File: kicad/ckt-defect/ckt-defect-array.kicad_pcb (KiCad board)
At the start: 2 copper layers, 114.3 x 188 mm, 307 parts, among them J1 Screw_Terminal_01x02, J10 Micro_SD_Card_Det_Hirose_DM3AT, J11 690-005-299-043, J12 SM04B-SRSS, J13 Conn_01x03, J14 Conn_01x03, J2 SM04B-SRSS, J3 SM04B-SRSS, J4 SM04B-SRSS, J5 SM04B-SRSS, J6 SM04B-SRSS, J7 SM04B-SRSS, J8 SM04B-SRSS, J9 Screw_Terminal_01x02, SW5 FSM4JSMA, SW6 FSM4JSMA, U1 MAX98357AETE+T, U2 AP63205WU, U3 TMP1075D, U4 AZ1117-3.3, U5 ESP32-S2-SOLO, U6 74LVC14, U7 TLP241A

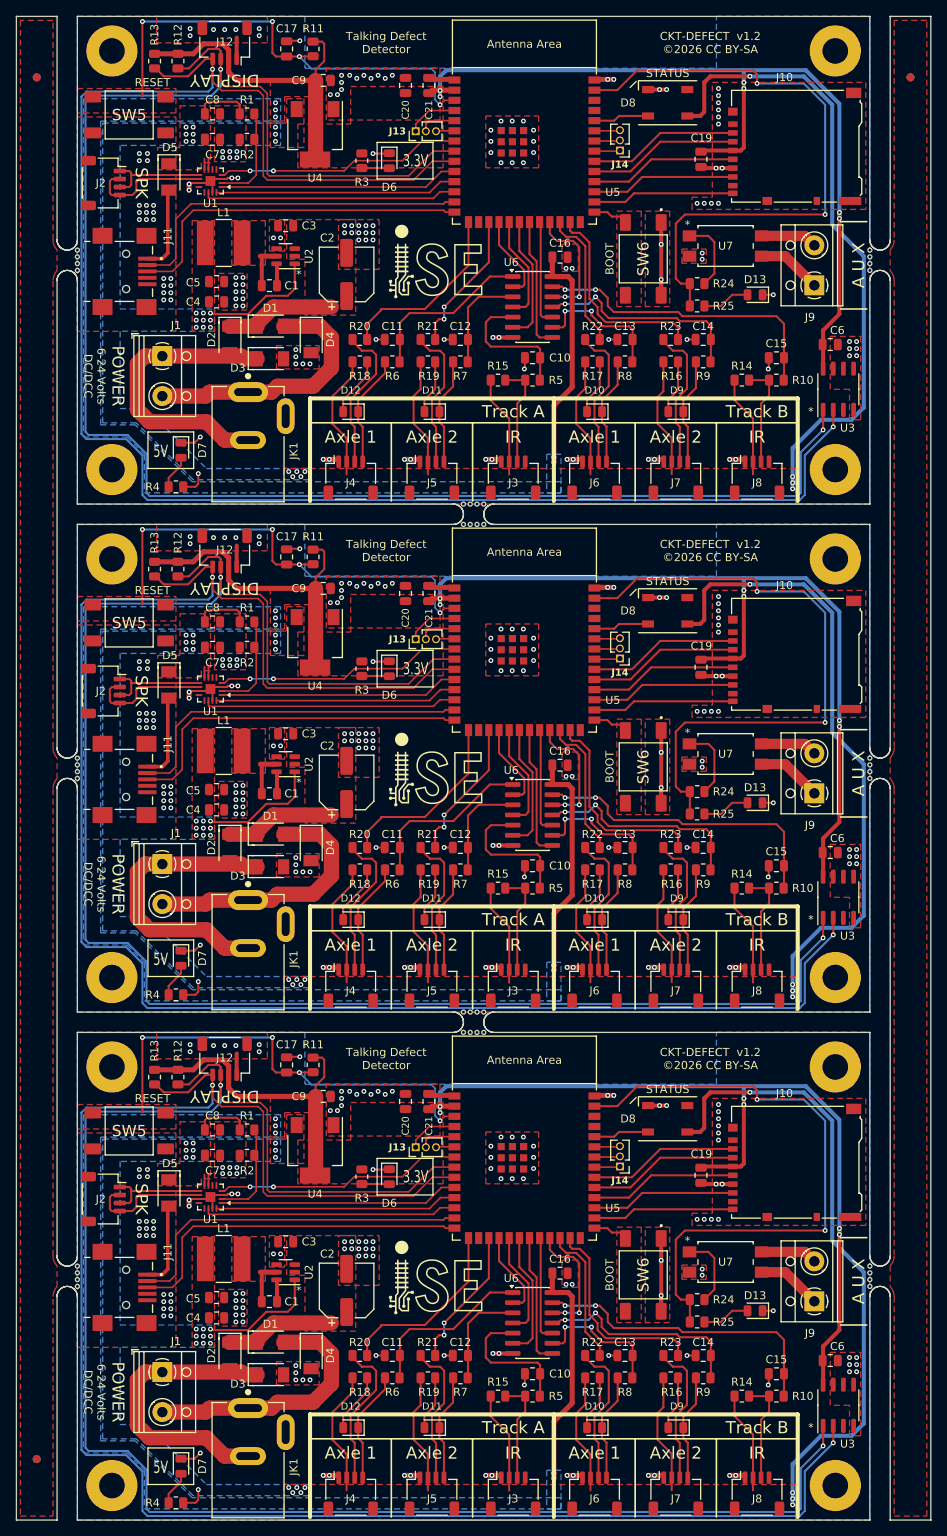
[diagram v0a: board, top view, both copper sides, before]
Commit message: Added fiducials
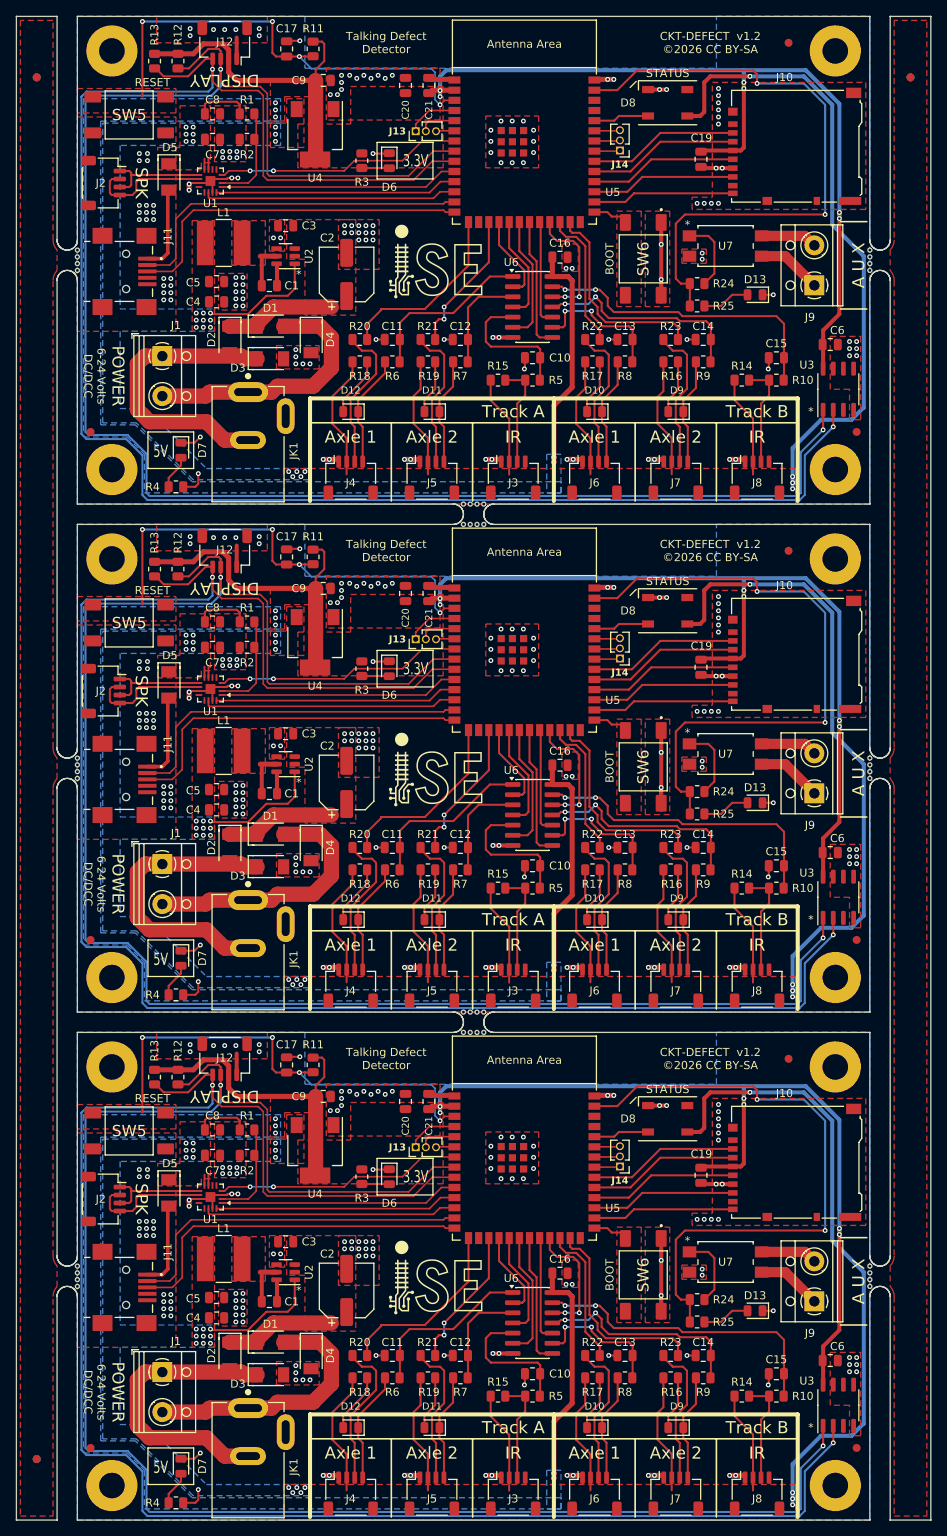
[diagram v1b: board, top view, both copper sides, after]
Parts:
- added FID1: Fiducial, Fiducial:Fiducial_1mm_Mask2mm, F.Cu at (187.9, 150.3)
- added FID1: Fiducial, Fiducial:Fiducial_1mm_Mask2mm, F.Cu at (187.9, 86.8)
- added FID1: Fiducial, Fiducial:Fiducial_1mm_Mask2mm, F.Cu at (187.9, 23.3)
- added FID2: Fiducial, Fiducial:Fiducial_1mm_Mask2mm, F.Cu at (100.6, 198.9)
- added FID2: Fiducial, Fiducial:Fiducial_1mm_Mask2mm, F.Cu at (100.6, 135.4)
- added FID2: Fiducial, Fiducial:Fiducial_1mm_Mask2mm, F.Cu at (100.6, 71.9)
- added FID3: Fiducial, Fiducial:Fiducial_1mm_Mask2mm, F.Cu at (196.4, 71.9)
- added FID3: Fiducial, Fiducial:Fiducial_1mm_Mask2mm, F.Cu at (196.4, 198.9)
- added FID3: Fiducial, Fiducial:Fiducial_1mm_Mask2mm, F.Cu at (196.4, 135.4)

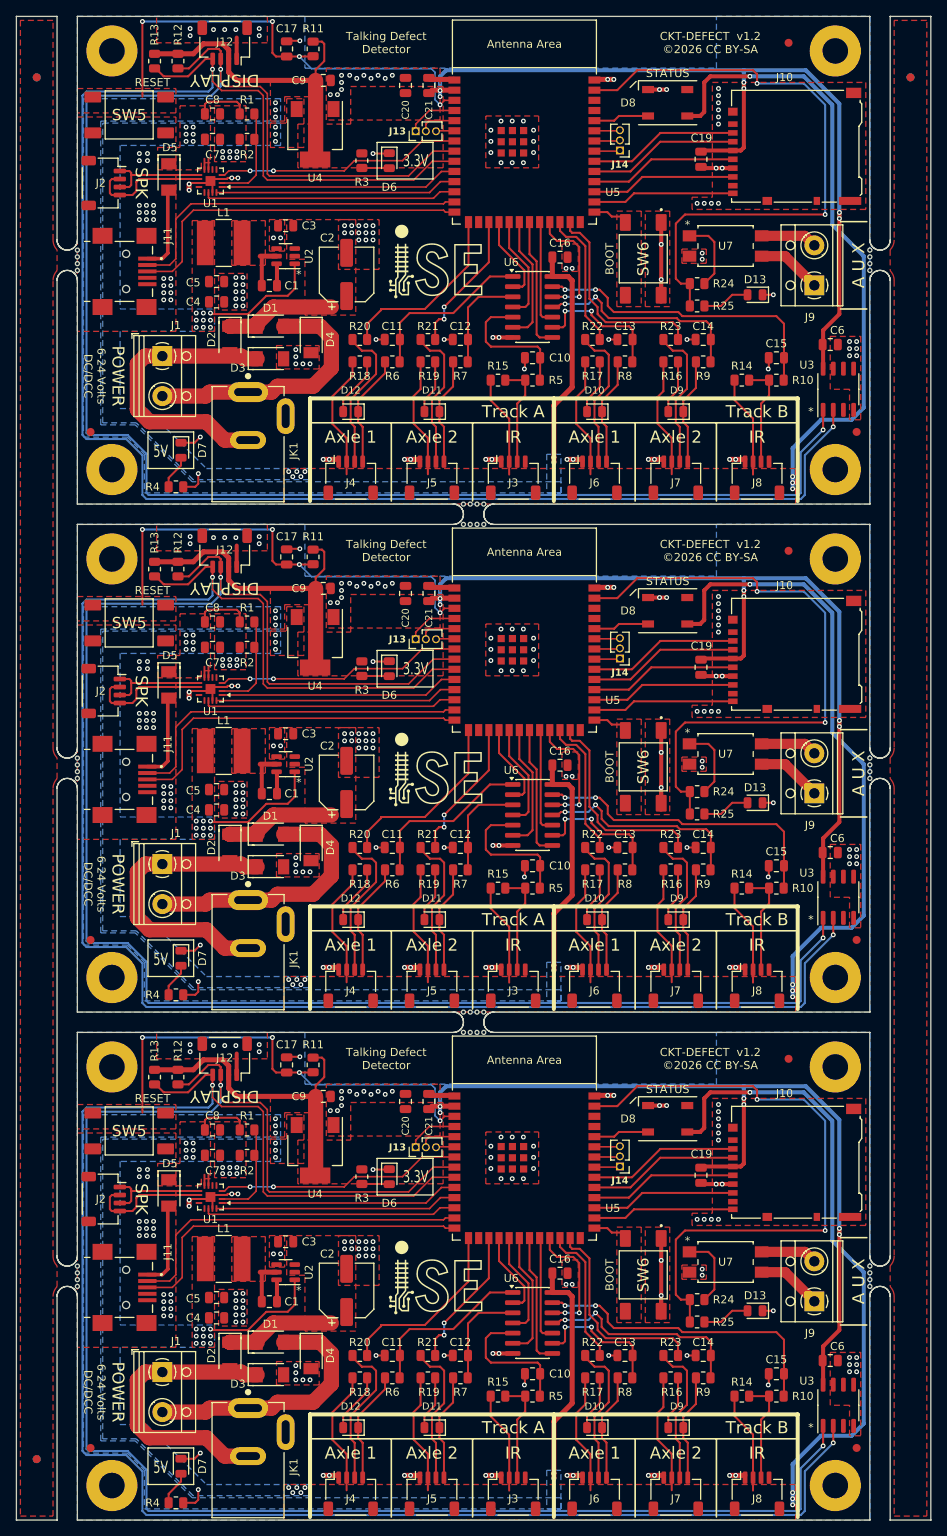
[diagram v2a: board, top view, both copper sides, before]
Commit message: Update tabs to get away from overhangs and delicate stuff
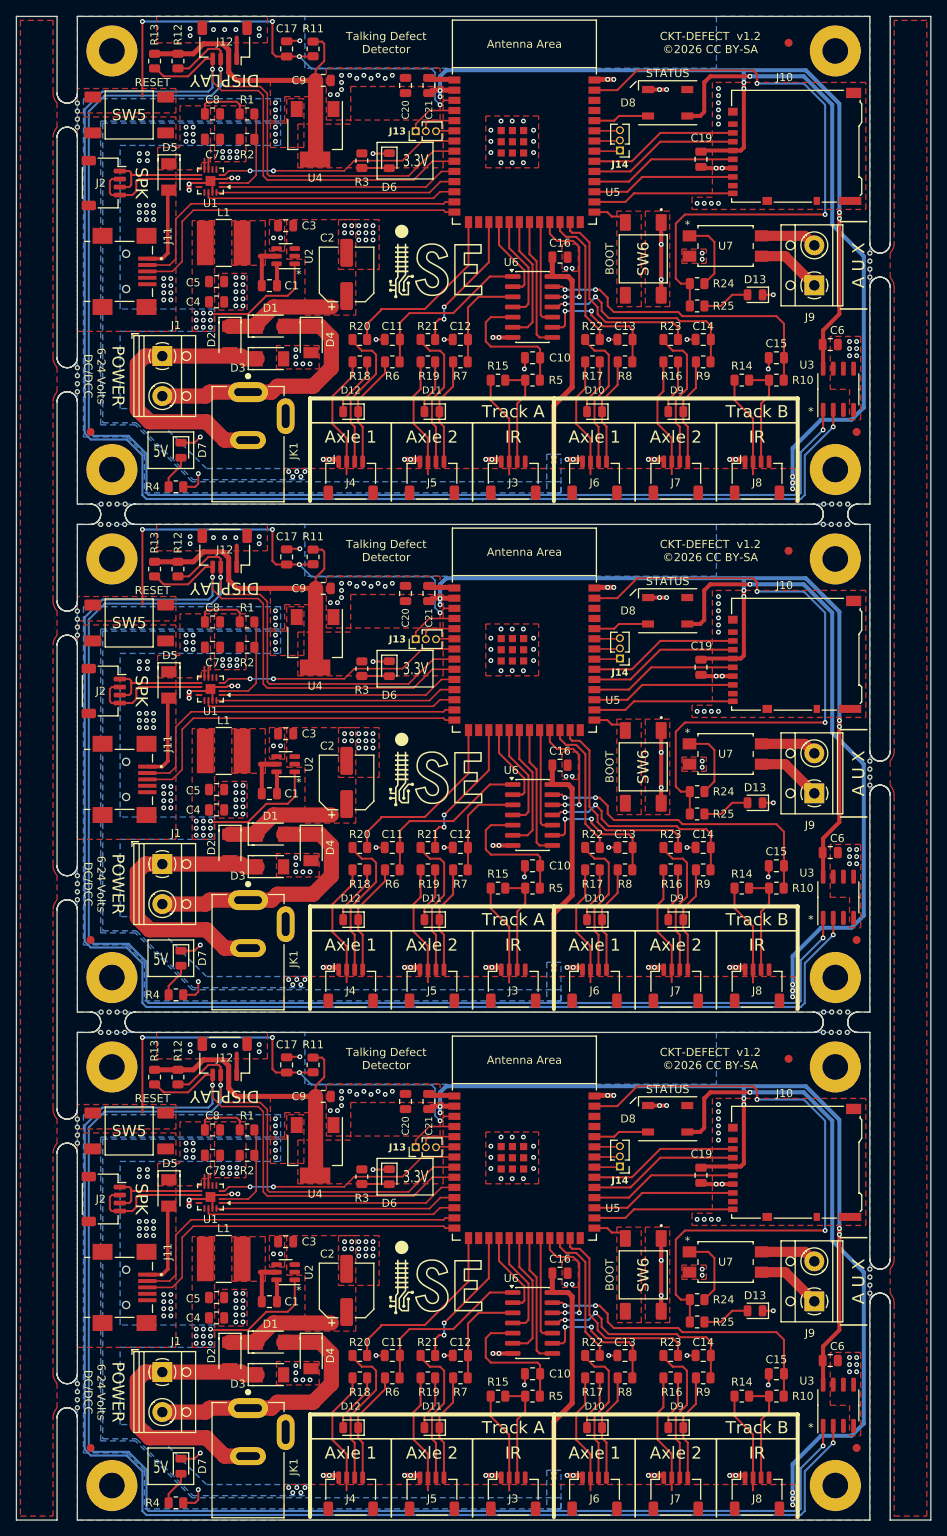
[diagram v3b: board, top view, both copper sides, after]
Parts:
- removed KiKit_FID_B_1, KiKit_FID_B_2, KiKit_FID_B_3, KiKit_FID_T_1, KiKit_FID_T_2, KiKit_FID_T_3: Fiducial, Fiducial
- added KiKit_MB_11_1: NPTH, NPTH, F.Cu at (198.0, 113.1)
- added KiKit_MB_11_2: NPTH, NPTH, F.Cu at (198.0, 114.1)
- added KiKit_MB_11_3: NPTH, NPTH, F.Cu at (198.0, 115.1)
- added KiKit_MB_11_4: NPTH, NPTH, F.Cu at (198.0, 116.1)
- added KiKit_MB_12_1: NPTH, NPTH, F.Cu at (99.0, 130.4)
- added KiKit_MB_12_2: NPTH, NPTH, F.Cu at (99.0, 129.4)
- added KiKit_MB_12_3: NPTH, NPTH, F.Cu at (99.0, 128.4)
- added KiKit_MB_12_4: NPTH, NPTH, F.Cu at (99.0, 127.4)
- added KiKit_MB_13_1: NPTH, NPTH, F.Cu at (192.2, 147.0)
- added KiKit_MB_13_2: NPTH, NPTH, F.Cu at (193.2, 147.0)
- added KiKit_MB_13_3: NPTH, NPTH, F.Cu at (194.2, 147.0)
- added KiKit_MB_13_4: NPTH, NPTH, F.Cu at (195.2, 147.0)
- added KiKit_MB_14_1: NPTH, NPTH, F.Cu at (99.0, 160.8)
- added KiKit_MB_14_2: NPTH, NPTH, F.Cu at (99.0, 159.8)
- added KiKit_MB_14_3: NPTH, NPTH, F.Cu at (99.0, 158.8)
- added KiKit_MB_14_4: NPTH, NPTH, F.Cu at (99.0, 157.8)
- added KiKit_MB_15_1: NPTH, NPTH, F.Cu at (101.9, 147.0)
- added KiKit_MB_15_2: NPTH, NPTH, F.Cu at (102.9, 147.0)
- added KiKit_MB_15_3: NPTH, NPTH, F.Cu at (103.9, 147.0)
- added KiKit_MB_15_4: NPTH, NPTH, F.Cu at (104.9, 147.0)
- added KiKit_MB_16_1: NPTH, NPTH, F.Cu at (198.0, 176.6)
- added KiKit_MB_16_2: NPTH, NPTH, F.Cu at (198.0, 177.6)
- added KiKit_MB_16_3: NPTH, NPTH, F.Cu at (198.0, 178.6)
- added KiKit_MB_16_4: NPTH, NPTH, F.Cu at (198.0, 179.6)
- added KiKit_MB_17_1: NPTH, NPTH, F.Cu at (99.0, 193.9)
- added KiKit_MB_17_2: NPTH, NPTH, F.Cu at (99.0, 192.9)
- added KiKit_MB_17_3: NPTH, NPTH, F.Cu at (99.0, 191.9)
- added KiKit_MB_17_4: NPTH, NPTH, F.Cu at (99.0, 190.9)
- moved KiKit_MB_9_4 130.1 mm to (99.0, 94.3)
- moved KiKit_MB_9_3 129.0 mm to (99.0, 95.3)
- moved KiKit_MB_9_2 127.8 mm to (99.0, 96.3)
- moved KiKit_MB_9_1 126.6 mm to (99.0, 97.3)
- moved KiKit_MB_4_1 118.8 mm to (198.0, 49.6)
- moved KiKit_MB_4_2 117.8 mm to (198.0, 50.6)
- moved KiKit_MB_4_3 116.8 mm to (198.0, 51.6)
- moved KiKit_MB_4_4 115.9 mm to (198.0, 52.6)
- moved KiKit_MB_5_4 111.6 mm to (99.0, 63.9)
- moved KiKit_MB_5_3 110.7 mm to (99.0, 64.9)
- moved KiKit_MB_5_2 109.9 mm to (99.0, 65.9)
- moved KiKit_MB_5_1 109.1 mm to (99.0, 66.9)
- moved KiKit_MB_8_1 102.2 mm to (195.3, 144.5)
- moved KiKit_MB_8_2 101.0 mm to (194.3, 144.5)
- moved KiKit_MB_8_3 99.8 mm to (193.3, 144.5)
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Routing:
- net Board_0-/SCL: track 223.5 -> 221.8 mm
- net Board_2-/SCL: track 223.5 -> 221.8 mm
- net Board_1-/SCL: track 223.5 -> 221.8 mm
- net Board_2-/SDA: track 219.9 -> 218.3 mm
- net Board_1-/SDA: track 219.9 -> 218.3 mm
- net Board_0-/SDA: track 219.9 -> 218.3 mm
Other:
- outline, holes or cut-outs redrawn
